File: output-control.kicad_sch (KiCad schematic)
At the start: 57 parts, among them U16 ADS7828, U17 TCA9534PWR, U18 ADS7828

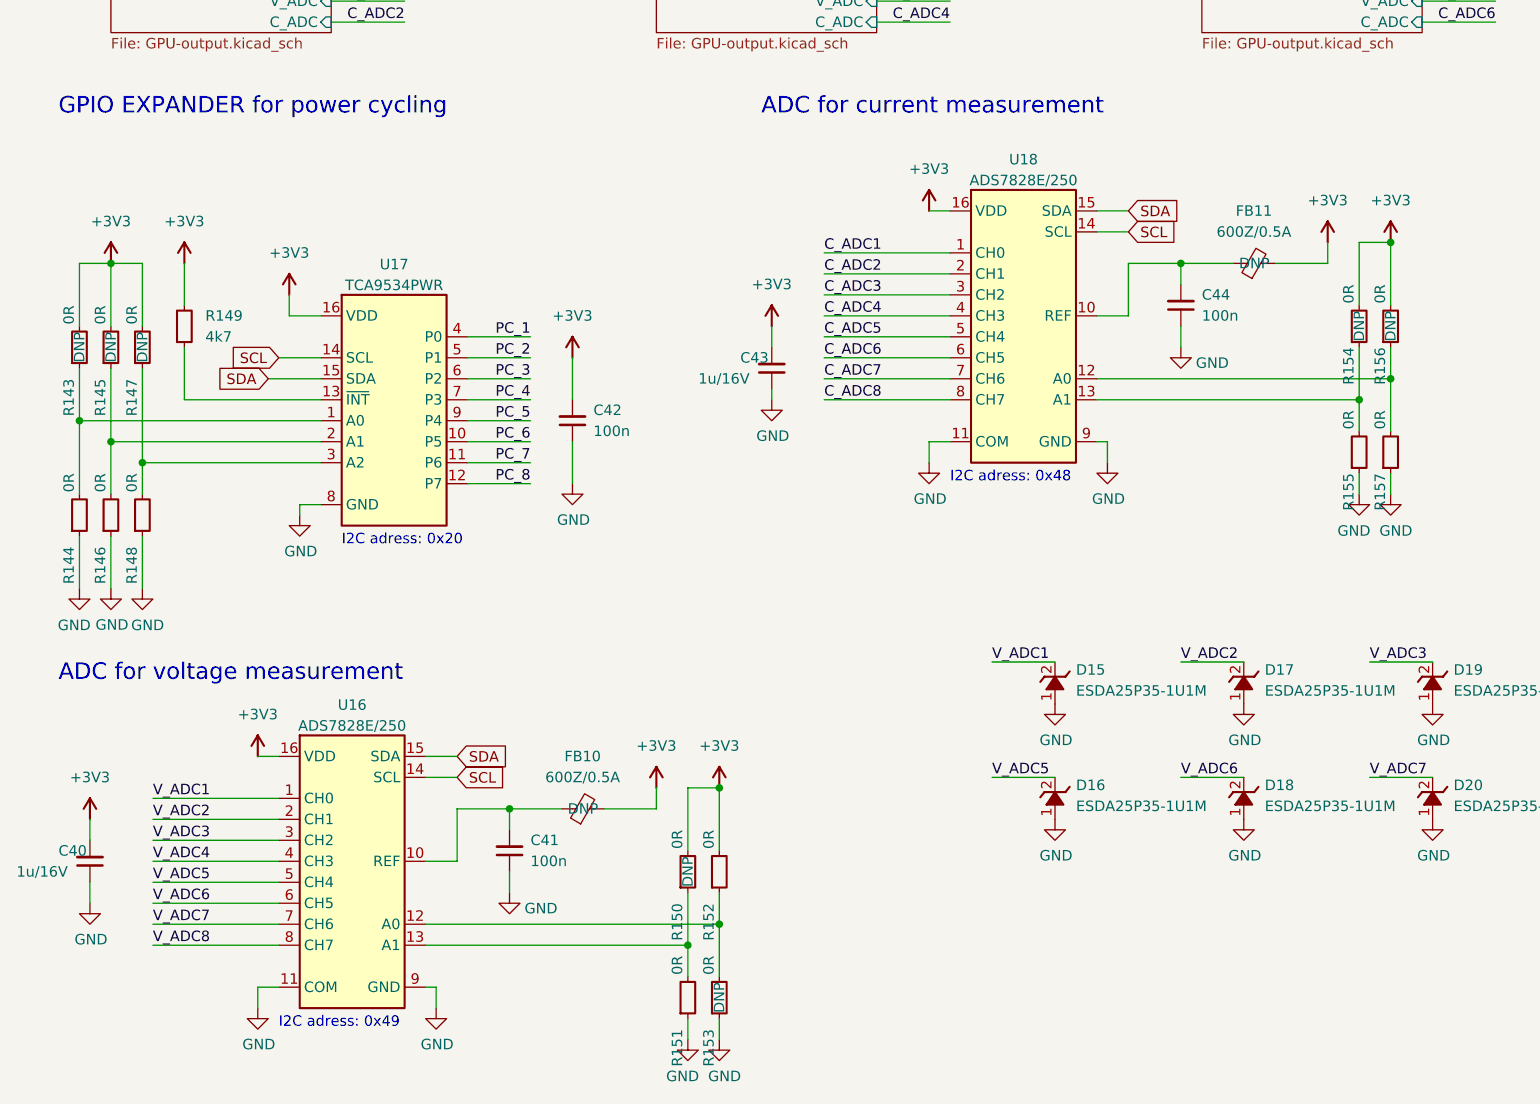
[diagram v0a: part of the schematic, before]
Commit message: Add mux for temp signals
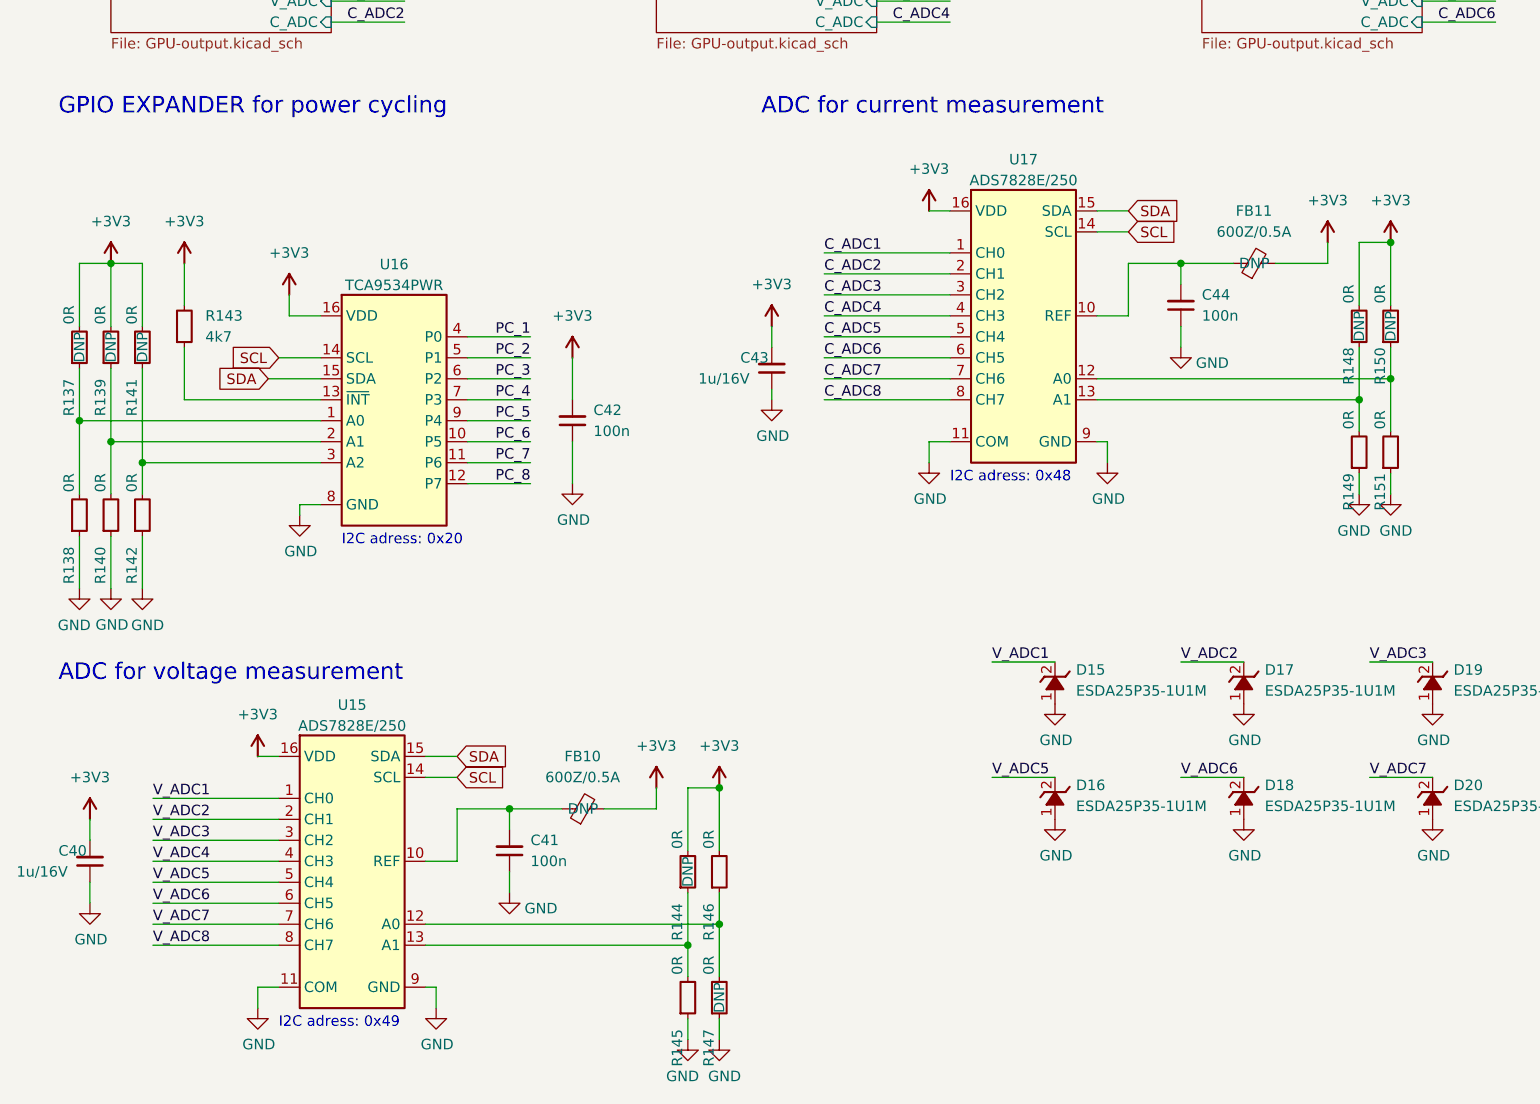
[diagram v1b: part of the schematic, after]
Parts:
- renumbered R143 to R137, R144 to R138, R145 to R139, R146 to R140, R147 to R141, R148 to R142, R149 to R143, R150 to R144, R151 to R145, R152 to R146, R153 to R147, R154 to R148, R155 to R149, R156 to R150, R157 to R151, U16 to U15, U17 to U16, U18 to U17

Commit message: Reannotate
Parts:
- renumbered C40 to C41, C41 to C42, C42 to C43, C43 to C44, C44 to C45

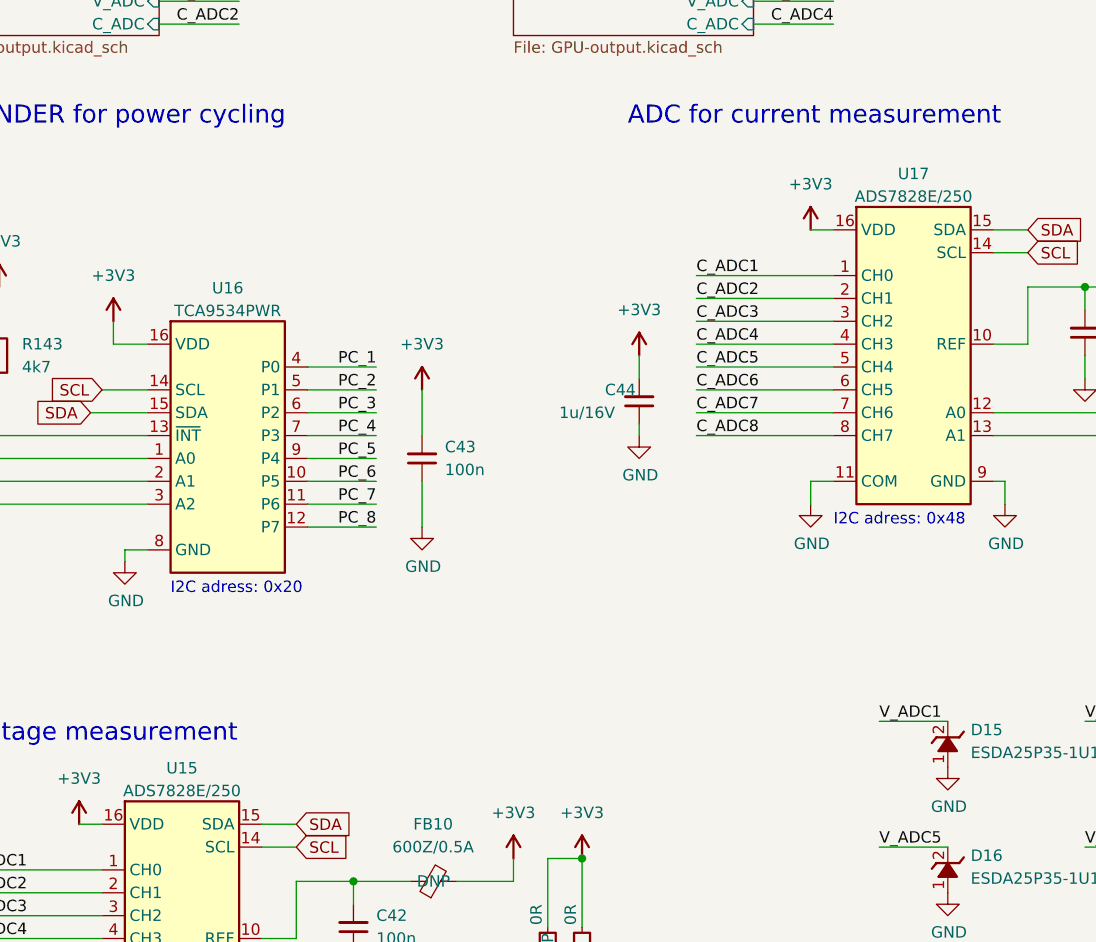
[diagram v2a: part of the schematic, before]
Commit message: Standarize all components and enumerate
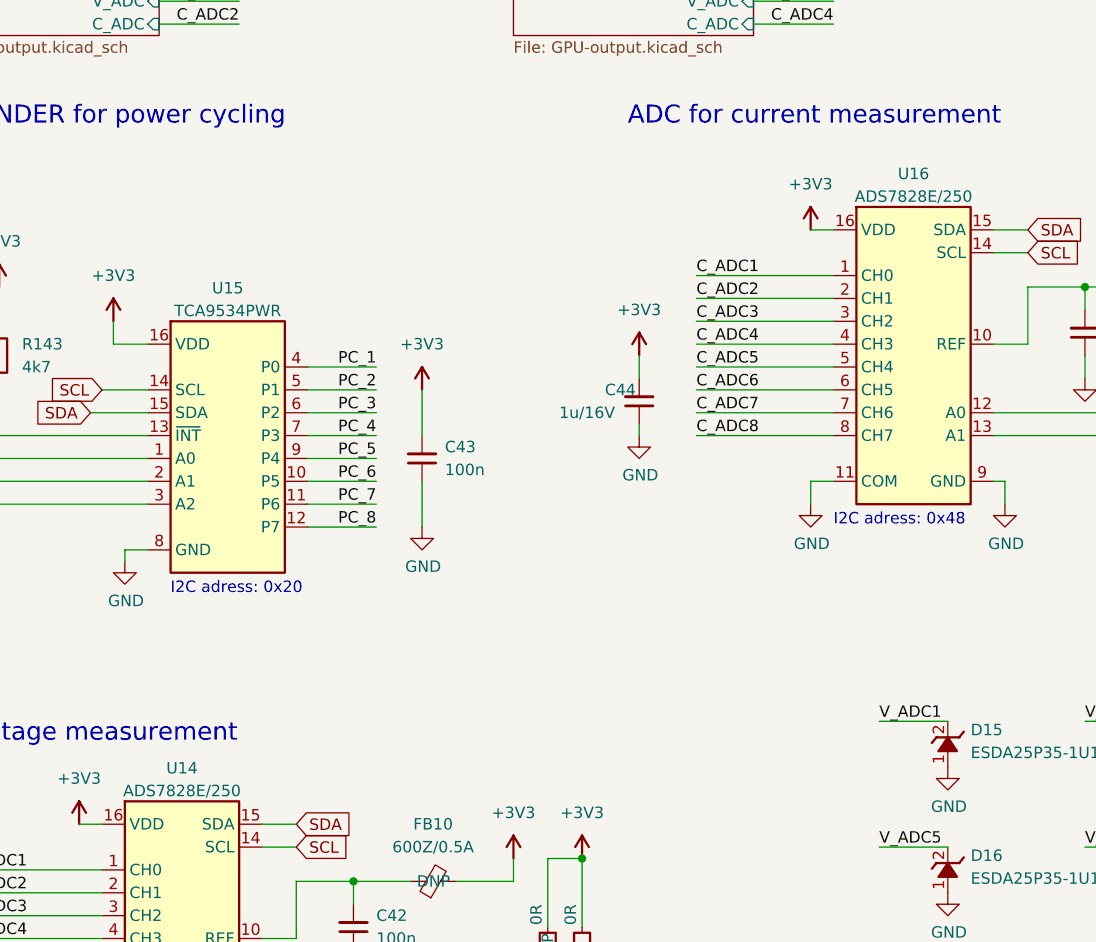
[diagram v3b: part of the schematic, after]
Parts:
- renumbered U15 to U14, U16 to U15, U17 to U16

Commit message: Reannotate
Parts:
- renumbered C41 to C44, C42 to C45, C43 to C46, C44 to C47, C45 to C48, R137 to R145, R138 to R146, R139 to R147, R140 to R148, R141 to R149, R142 to R150, R143 to R151, R144 to R152, R145 to R153, R146 to R154, R147 to R155, R148 to R156, R149 to R157, R150 to R158, R151 to R159, U14 to U17, U15 to U18, U16 to U19

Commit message: Cosmetic changes and added adnotations
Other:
- note added: "Invidual channels for connecting thunderbolt-gpu-adapters"
- moved on the sheet: C44, C45, C46, C47, C48, D15, D16, D17, D18, D19, D20, D21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

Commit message: Additional cleanup
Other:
- title: (none) -> GPU Cluster Backplane
- moved on the sheet: C44, C45, C46, C47, C48, D15, D16, D17, D18, D19, D20, D21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

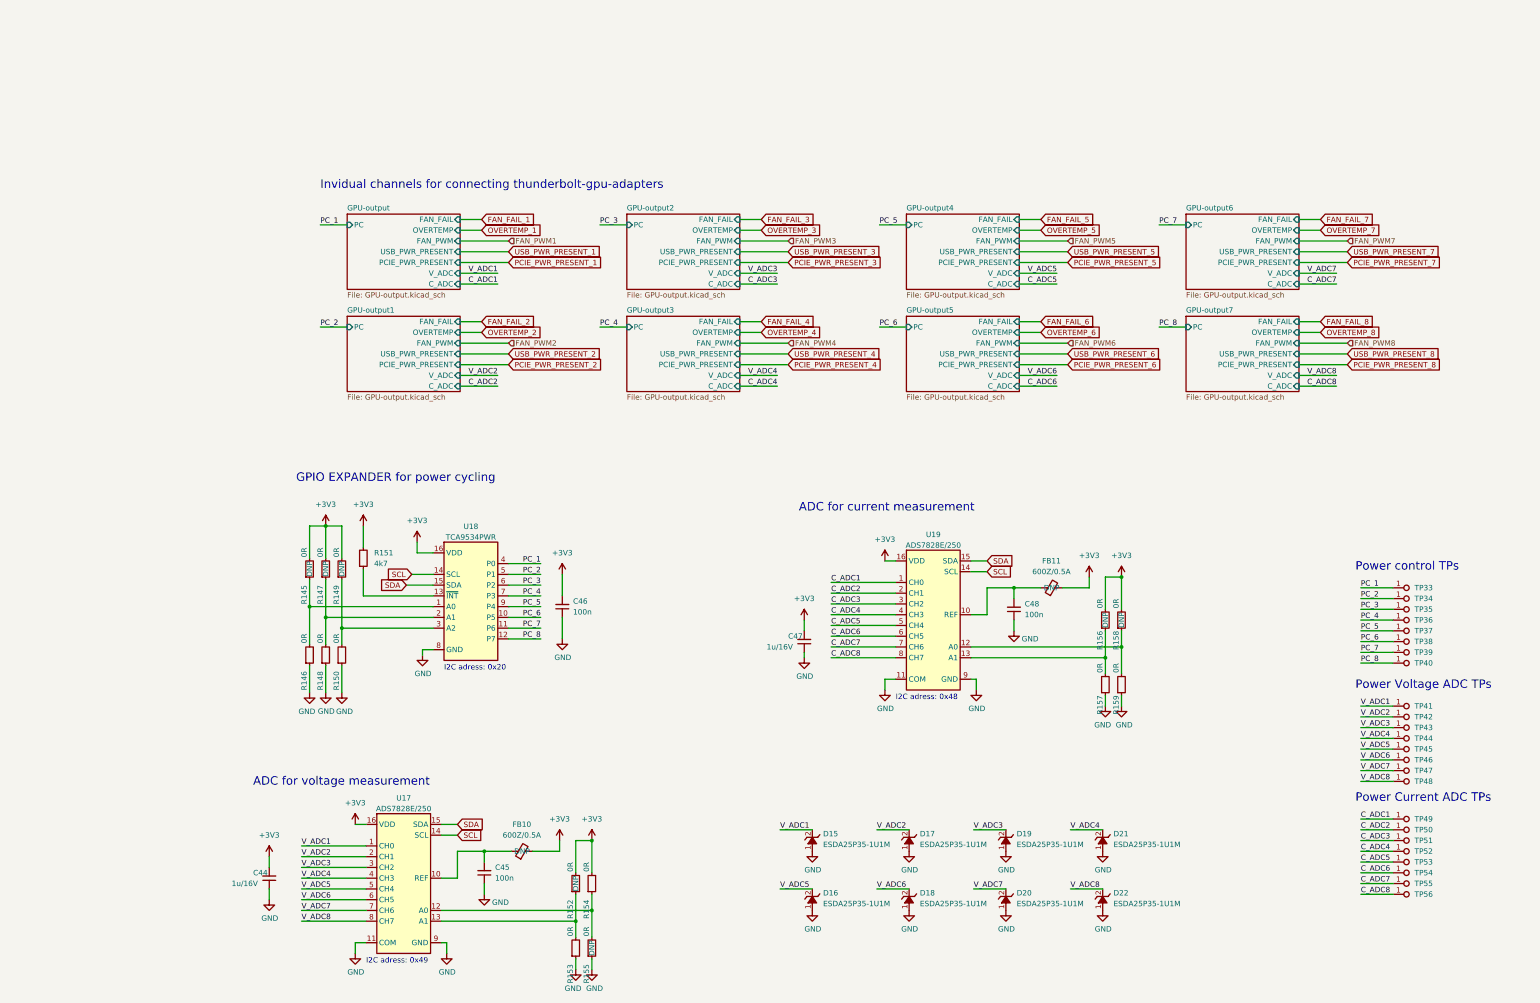
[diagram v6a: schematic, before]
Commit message: Minor fixes in schematic layout and reannotate
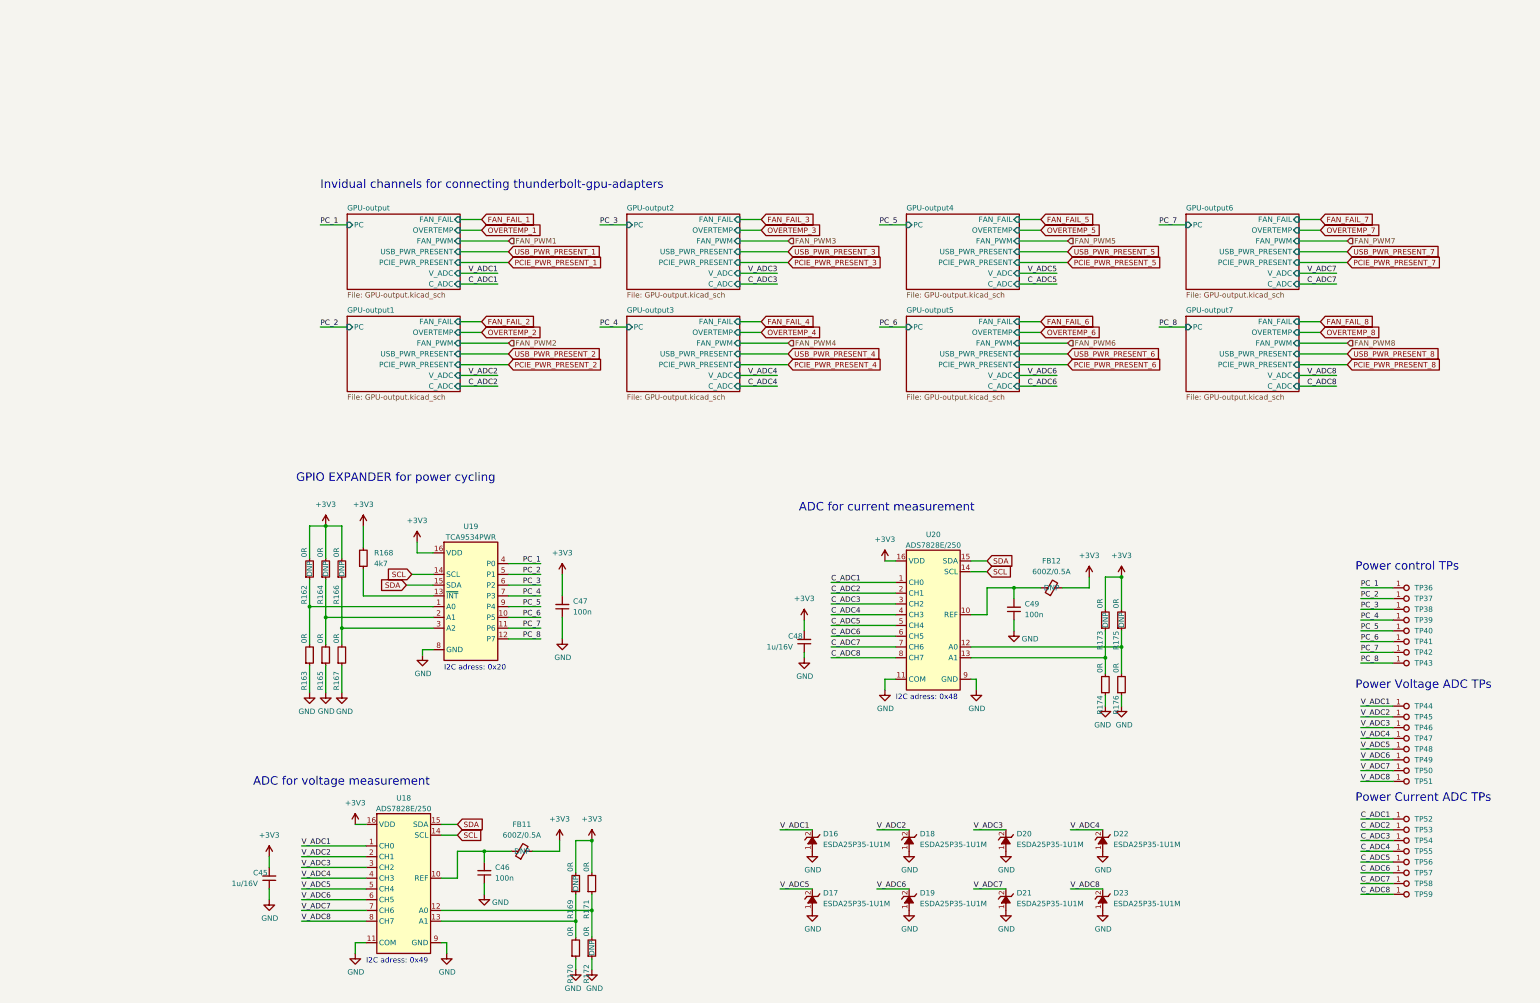
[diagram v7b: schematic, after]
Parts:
- renumbered C44 to C45, C45 to C46, C46 to C47, C47 to C48, C48 to C49, D15 to D16, D16 to D17, D17 to D18, D18 to D19, D19 to D20, D20 to D21, D21 to D22, D22 to D23, FB10 to FB11, FB11 to FB12, R145 to R162, R146 to R163, R147 to R164, R148 to R165, R149 to R166, R150 to R167, R151 to R168, R152 to R169, R153 to R170, R154 to R171, R155 to R172, R156 to R173, R157 to R174, R158 to R175, R159 to R176, TP33 to TP36, TP34 to TP37, TP35 to TP38, TP36 to TP39, TP37 to TP40, TP38 to TP41, TP39 to TP42, TP40 to TP43, TP41 to TP44, TP42 to TP45, TP43 to TP46, TP44 to TP47, TP45 to TP48, TP46 to TP49, TP47 to TP50, TP48 to TP51, TP49 to TP52, TP50 to TP53, TP51 to TP54, TP52 to TP55, TP53 to TP56, TP54 to TP57, TP55 to TP58, TP56 to TP59, U17 to U18, U18 to U19, U19 to U20
